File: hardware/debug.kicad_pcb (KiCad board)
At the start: 2 copper layers, 40 x 40 mm, 26 parts, among them J1 STACK-DOWN, J2 USB-MINI-B-SMD, J3 STACK-DOWN, P1 CONN_16, P2 JTAG, U1 CM1293A, U2 CP2104, U3 DRILL, U4 DRILL, U5 DRILL

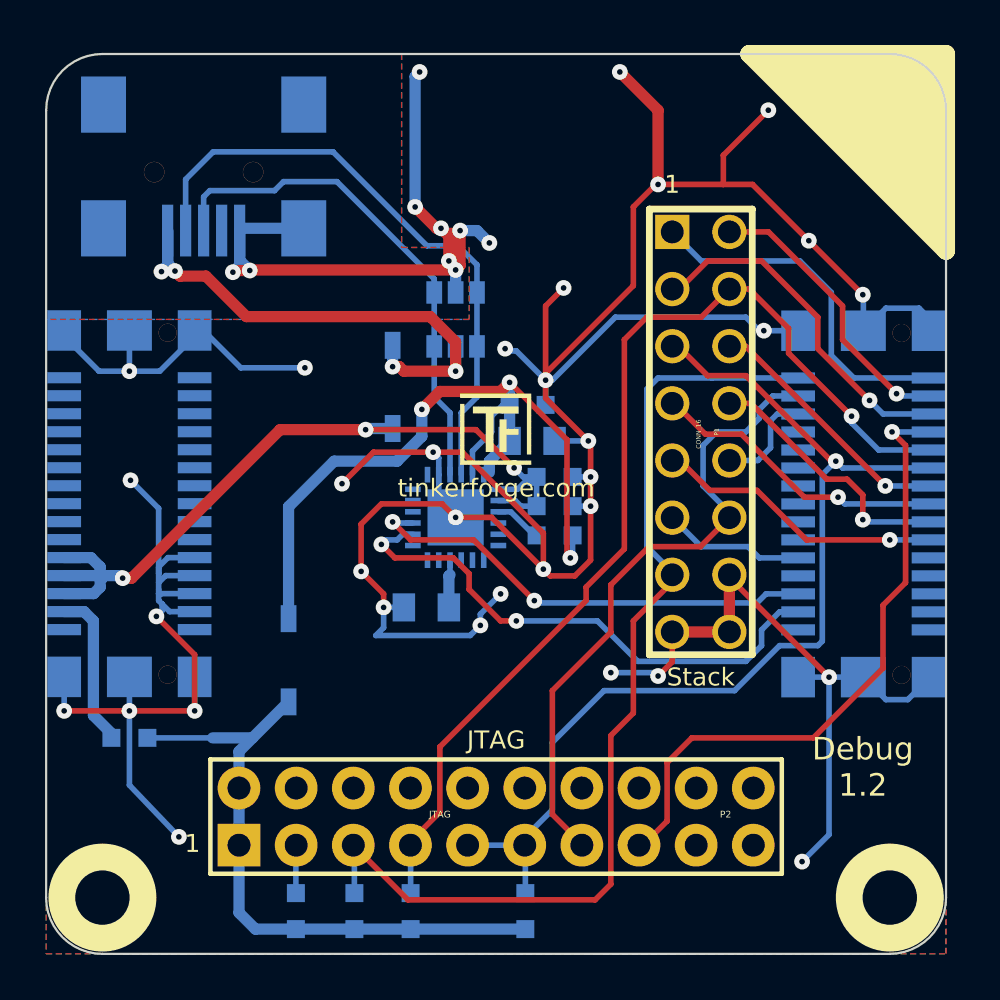
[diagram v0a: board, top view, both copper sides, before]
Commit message: Add all 3d information
move conn components to kicad-libraries
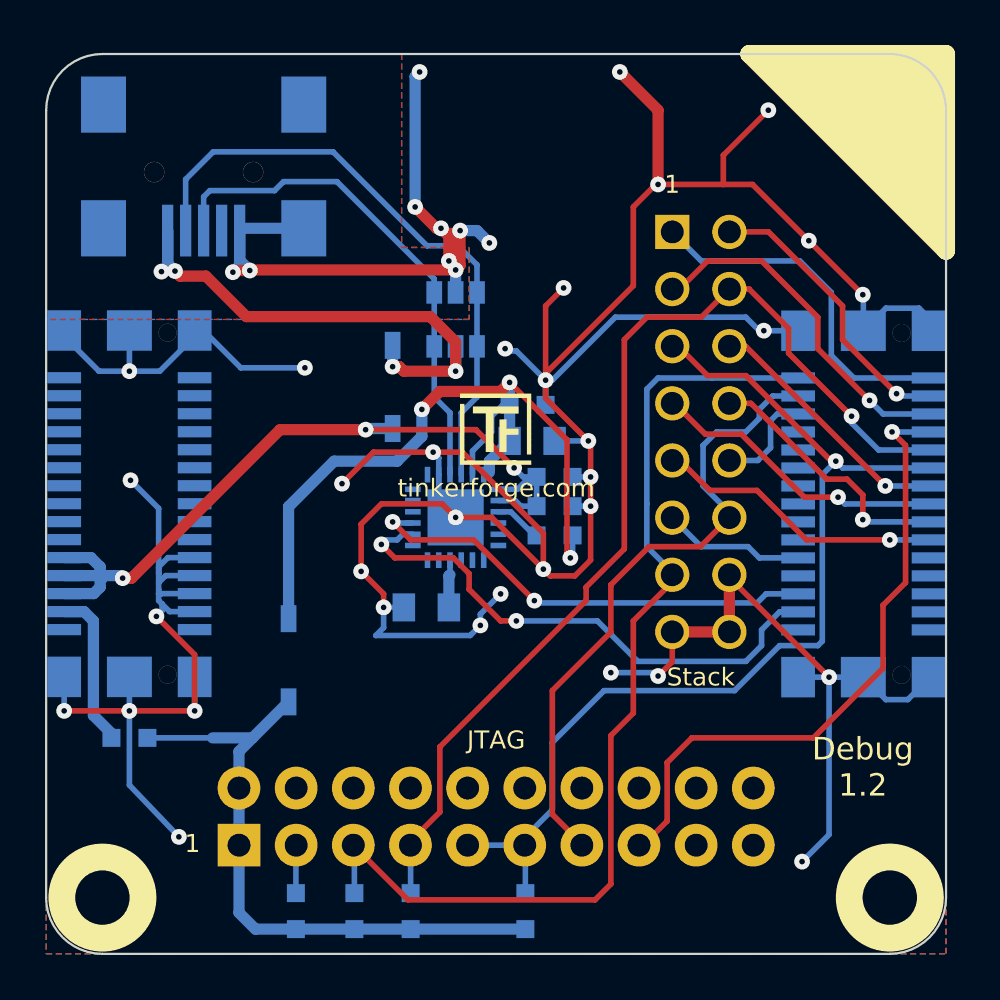
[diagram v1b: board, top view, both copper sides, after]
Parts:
- C1, C2, C5: footprint 0603 -> C0603
- C3, C4: footprint 0805 -> C0805
- G***: footprint Logo_31x31 -> kicad-libraries:Logo_31x31
- P2: footprint tinkerforge:PIN_ARRAY_10x2 -> pin_array_10x2
- R1, R2, R3, R4, R5, R6: footprint 0603 -> R0603
- U2: footprint QFN-24-4x4-EP -> kicad-libraries:QFN-24-4x4-EP
- VAL: footprint CE_5mm -> kicad-libraries:CE_5mm
- VAL: footprint WEEE_7mm -> kicad-libraries:WEEE_7mm
- turned VAL to 180 degrees
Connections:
- net +3.3V renamed +3V3
- J1 pad 10: (no net) -> Net-(J1-Pad10)
- J1 pad 12: (no net) -> Net-(J1-Pad12)
- J1 pad 14: (no net) -> Net-(J1-Pad14)
- J1 pad 16: (no net) -> Net-(J1-Pad16)
- J1 pad 18: (no net) -> Net-(J1-Pad18)
- J1 pad 20: (no net) -> Net-(J1-Pad20)
- J1 pad 21: (no net) -> Net-(J1-Pad21)
- J1 pad 23: (no net) -> Net-(J1-Pad23)
- J1 pad 24: (no net) -> Net-(J1-Pad24)
- J1 pad 25: (no net) -> Net-(J1-Pad25)
- J1 pad 27: (no net) -> Net-(J1-Pad27)
- J1 pad 29: (no net) -> Net-(J1-Pad29)
- J1 pad 30: (no net) -> Net-(J1-Pad30)
- J1 pad 8: (no net) -> Net-(J1-Pad8)
- J2 pad 4: (no net) -> Net-(J2-Pad4)
- J3 pad 1: (no net) -> Net-(J3-Pad1)
- J3 pad 10: (no net) -> Net-(J3-Pad10)
- J3 pad 11: (no net) -> Net-(J3-Pad11)
- J3 pad 12: (no net) -> Net-(J3-Pad12)
- J3 pad 13: (no net) -> Net-(J3-Pad13)
- J3 pad 14: (no net) -> Net-(J3-Pad14)
- J3 pad 15: (no net) -> Net-(J3-Pad15)
- J3 pad 16: (no net) -> Net-(J3-Pad16)
- J3 pad 17: (no net) -> Net-(J3-Pad17)
- J3 pad 18: (no net) -> Net-(J3-Pad18)
- J3 pad 19: (no net) -> Net-(J3-Pad19)
- J3 pad 2: (no net) -> Net-(J3-Pad2)
- J3 pad 20: (no net) -> Net-(J3-Pad20)
- J3 pad 29: (no net) -> Net-(J3-Pad29)
- J3 pad 3: (no net) -> Net-(J3-Pad3)
- J3 pad 30: (no net) -> Net-(J3-Pad30)
- J3 pad 4: (no net) -> Net-(J3-Pad4)
- J3 pad 5: (no net) -> Net-(J3-Pad5)
- J3 pad 6: (no net) -> Net-(J3-Pad6)
- J3 pad 7: (no net) -> Net-(J3-Pad7)
- J3 pad 8: (no net) -> Net-(J3-Pad8)
- J3 pad 9: (no net) -> Net-(J3-Pad9)
- P2 pad 17: (no net) -> Net-(P2-Pad17)
- P2 pad 19: (no net) -> Net-(P2-Pad19)
- U2 pad 1: (no net) -> Net-(U2-Pad1)
- U2 pad 10: (no net) -> Net-(U2-Pad10)
- U2 pad 11: (no net) -> Net-(U2-Pad11)
- U2 pad 12: (no net) -> Net-(U2-Pad12)
- U2 pad 13: (no net) -> Net-(U2-Pad13)
- U2 pad 14: (no net) -> Net-(U2-Pad14)
- U2 pad 15: (no net) -> Net-(U2-Pad15)
- U2 pad 17: (no net) -> Net-(U2-Pad17)
- U2 pad 18: (no net) -> Net-(U2-Pad18)
- U2 pad 19: (no net) -> Net-(U2-Pad19)
- U2 pad 22: (no net) -> Net-(U2-Pad22)
- U2 pad 23: (no net) -> Net-(U2-Pad23)
- U2 pad 24: (no net) -> Net-(U2-Pad24)

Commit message: Add new 3d model
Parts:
- J1, J3: footprint BTB08-ACS-BTM -> kicad-libraries:BTB08-ACS-BTM
- J2: footprint USB-MINI-B-SMD -> kicad-libraries:USB-MINI-B-SMD
